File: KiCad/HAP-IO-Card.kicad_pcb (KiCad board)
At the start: 2 copper layers, 110 x 72 mm, 203 parts, among them CON601 AVR-JTAG-10, J201 TE_Connectivity_1-282834-0, J202 TE_Connectivity_282834-6, J203 TE_Connectivity_282834-6, J204 TE_Connectivity_1-282834-0, J401 TE_Connectivity_1-282834-0, J402 TE_Connectivity_282834-6, J501 TE_Connectivity_282834-3, J502 CONN_01X03_FEMALE, J601 ISP0, J602 ISP1, J603 CONN_01X02, J604 CONN_01X02, J605 CONN_01X02, J606 CONN_01X02, J607 CONN_01X03, J608 CONN_01X03, J701 5V_I/O_2, J702 5V_I/O_1, J703 NEO1, J704 NEO2, J705 NEO3, J706 NEO4, J707 CONN_01X03, Q201 ZXTN25050DFHTA, Q202 ZXTN25050DFHTA, Q203 ZXTN25050DFHTA, Q204 ZXTN25050DFHTA, Q205 ZXTN25050DFHTA, Q206 ZXTN25050DFHTA, Q207 ZXTN25050DFHTA, Q208 ZXTN25050DFHTA, U201 LTV-354T, U202 LTV-354T, U203 LTV-354T, U204 LTV-354T, U205 LTV-354T, U206 LTV-354T, U207 LTV-354T, U208 LTV-354T, U209 MCP23017, U401 ADS1115IDGST, U402 ADS1115IDGST, U501 LM1086-5V, U502 LM1086-3.3V, U701 TXB0102DCT

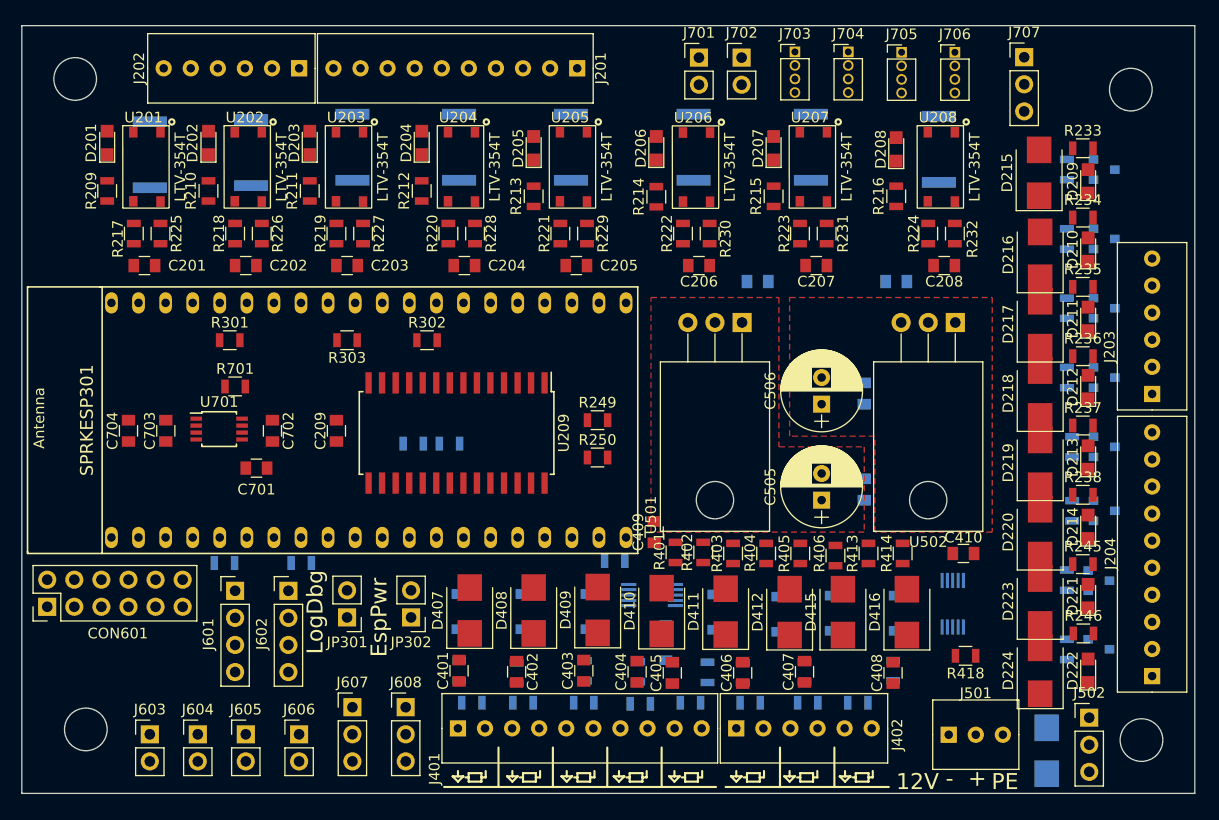
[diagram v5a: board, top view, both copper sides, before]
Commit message: Halfway through routing - need better layout to prevent rats nest
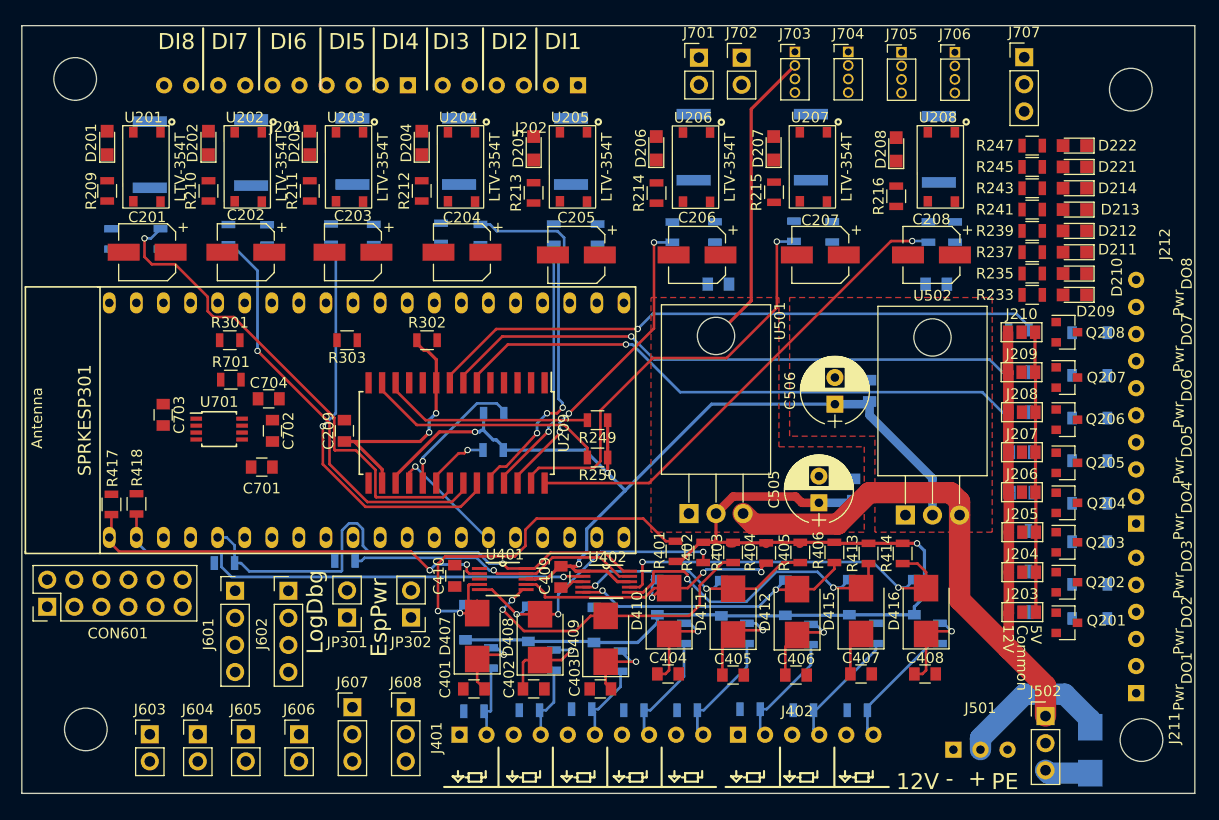
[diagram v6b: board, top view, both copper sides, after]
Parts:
- added J205: GS3, Connectors:GS3, F.Cu at (131.1, 65.0)
- added J206: GS3, Connectors:GS3, F.Cu at (131.0, 61.2)
- added J207: GS3, Connectors:GS3, F.Cu at (131.0, 57.5)
- added J208: GS3, Connectors:GS3, F.Cu at (131.0, 53.7)
- added J209: GS3, Connectors:GS3, F.Cu at (131.0, 50.0)
- added J210: GS3, Connectors:GS3, F.Cu at (131.0, 46.2)
- added J211: TE_Connectivity_282834-6, TE_Connectivity:TE_Connectivity_282834-6, F.Cu at (141.7, 80.1)
- added J212: TE_Connectivity_1-282834-0, TE_Connectivity:TE_Connectivity_1-282834-0, F.Cu at (141.7, 64.2)
- C201, C202, C203, C204, C205, C206, C207, C208: footprint Capacitors_SMD:C_0805 -> Capacitors_SMD:CP_Elec_5x4.5
- C505, C506: footprint Capacitors_THT:CP_Radial_D7.5mm_P2.50mm -> Capacitors_THT:CP_Radial_D6.3mm_P2.50mm
- D215, D216, D217, D218, D219, D220, D223, D224: value S1BB-13-F -> MBR0580; footprint Diodes_SMD:D_SMB -> Diodes_SMD:D_SOD-123; moved to B.Cu
- J203: value TE_Connectivity_282834-6 -> GS3; footprint TE_Connectivity:TE_Connectivity_282834-6 -> Connectors:GS3
- J204: value TE_Connectivity_1-282834-0 -> GS3; footprint TE_Connectivity:TE_Connectivity_1-282834-0 -> Connectors:GS3
- Q201, Q202, Q203, Q204, Q205, Q206, Q207, Q208, R417, U401, U402: moved to F.Cu
- R209, R210, R211, R212, R213, R214, R215, R216: value 180 -> 56
- R217, R218, R219, R220, R221, R222, R223, R224, R225, R226, R227, R228, R229, R230, R231, R232: moved to B.Cu
- R233, R235, R237, R245: value 180 -> 68
- R234, R236, R238, R246: value 180 -> 470; moved to B.Cu
- R239, R241, R243, R247: value 470 -> 68; moved to F.Cu
- moved R418 79.0 mm to (48.0, 62.3), turned to 270 degrees
- moved D222 49.3 mm to (136.0, 28.7), turned to 180 degrees
- moved C410 47.7 mm to (77.8, 69.1), turned to 270 degrees
- moved R417 47.5 mm to (45.6, 62.4), turned to 270 degrees
- moved Q201 42.6 mm to (135.2, 73.5)
- moved D215 42.1 mm to (137.4, 73.1), turned to 180 degrees
- moved R247 40.9 mm to (132.0, 28.7), turned to 0 degrees
- moved D221 40.3 mm to (136.0, 30.7), turned to 180 degrees
- moved R245 37.6 mm to (132.0, 30.7)
- moved R234 37.5 mm to (130.8, 72.5)
- moved U402 32.6 mm to (92.0, 69.6), turned to 0 degrees
- moved Q202 32.4 mm to (135.2, 69.7)
- moved D224 32.0 mm to (137.4, 46.3), turned to 180 degrees
- moved D214 31.8 mm to (136.0, 32.7), turned to 180 degrees
- moved D216 31.2 mm to (137.4, 69.9), turned to 180 degrees
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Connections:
- net /Powersupply/Input12VOutside renamed /Powersupply/12V_PWR
- C501 pad 1: /Powersupply/Input12V -> +12V
- C502 pad 1: /Powersupply/Input12V -> +12V
- D501 pad 1: +12V -> Net-(D501-Pad1)
- J203 pad 1: Earth -> POWER5V
- J203 pad 2: /Digital I/O/DO_1 -> /Digital I/O/PWR_DO_1
- J203 pad 3: Earth -> +12V
- J204 pad 1: Earth -> POWER5V
- J204 pad 2: /Digital I/O/DO_4 -> /Digital I/O/PWR_DO_2
- J204 pad 3: Earth -> +12V
- J502 pad 1: /Powersupply/Input12V -> +12V
- J502 pad 3: +12V -> Net-(D501-Pad1)
- R234 pad 1: POWER3V3 -> Net-(Q201-Pad1)
- R234 pad 2: Net-(D210-Pad2) -> DO1
- R235 pad 2: Net-(D211-Pad2) -> Net-(D210-Pad2)
- R236 pad 1: POWER3V3 -> Net-(Q202-Pad1)
- R236 pad 2: Net-(D212-Pad2) -> DO2
- R237 pad 2: Net-(D213-Pad2) -> Net-(D211-Pad2)
- R238 pad 1: POWER3V3 -> Net-(Q203-Pad1)
- R238 pad 2: Net-(D214-Pad2) -> DO3
- R239 pad 1: Net-(Q201-Pad1) -> POWER3V3
- R239 pad 2: DO1 -> Net-(D212-Pad2)
- R240 pad 1: Net-(Q202-Pad1) -> Net-(Q204-Pad1)
- R240 pad 2: DO2 -> DO4
- R241 pad 1: Net-(Q203-Pad1) -> POWER3V3
- R241 pad 2: DO3 -> Net-(D213-Pad2)
- R242 pad 1: Net-(Q204-Pad1) -> Net-(Q205-Pad1)
- R242 pad 2: DO4 -> DO5
- R243 pad 1: Net-(Q205-Pad1) -> POWER3V3
- R243 pad 2: DO5 -> Net-(D214-Pad2)
- R246 pad 1: POWER3V3 -> Net-(Q207-Pad1)
- R246 pad 2: Net-(D222-Pad2) -> DO7
- R247 pad 1: Net-(Q207-Pad1) -> POWER3V3
- R247 pad 2: DO7 -> Net-(D222-Pad2)
- U501 pad 3: /Powersupply/Input12V -> +12V
- U502 pad 3: /Powersupply/Input12V -> +12V
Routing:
- net POWER5V: track 0.00 -> 147.5 mm, vias 0 -> 1
- net POWER3V3: track 0.00 -> 117.8 mm, vias 0 -> 5
- net +12V: track 0.00 -> 75.5 mm
- net DO8: track 0.00 -> 58.2 mm, vias 0 -> 1
- net DO7: track 0.00 -> 54.7 mm, vias 0 -> 1
- net DO6: track 0.00 -> 54.4 mm, vias 0 -> 1
- net SENSE_SCL: track 0.00 -> 49.4 mm, vias 0 -> 1
- net SENSE_RDY_2: track 0.00 -> 46.6 mm, vias 0 -> 1
- net DI1: track 0.00 -> 46.5 mm, vias 0 -> 1
- net DI8: track 0.00 -> 45.4 mm, vias 0 -> 1
- net DI7: track 0.00 -> 40.9 mm, vias 0 -> 1
- net Sense1: track 0.00 -> 40.2 mm, vias 0 -> 2
- net DI2: track 0.00 -> 39.8 mm, vias 0 -> 1
- net SENSE_RDY_1: track 0.00 -> 39.4 mm, vias 0 -> 2
- net DI3: track 0.00 -> 38.8 mm, vias 0 -> 1
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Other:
- net class 12V added: clearance 0.2, trace_width 1, via_dia 0.6, via_drill 0.4
- net class 3V3: trace_width 0.25 -> 0.3
- net class 5V: trace_width 0.25 -> 0.3
- net class Earth added: clearance 0.2, trace_width 0.25, via_dia 0.6, via_drill 0.4
- net class Input12V removed
- net class Input12VOutside removed
- net class Input12VOutside2 removed
- board text added: "5V"
- board text added: "Common"
- board text added: "DI1"
- board text added: "DI2"
- board text added: "DI3"
- board text added: "DI4"
- board text added: "DI5"
- board text added: "DI6"
- board text added: "DI7"
- board text added: "DI8"
- board text added: "DO1"
- board text added: "DO2"
- board text added: "DO3"
- board text added: "DO4"
- board text added: "DO5"
- board text added: "DO6"
- board text added: "DO7"
- board text added: "DO8"
- board text added: "Pwr"

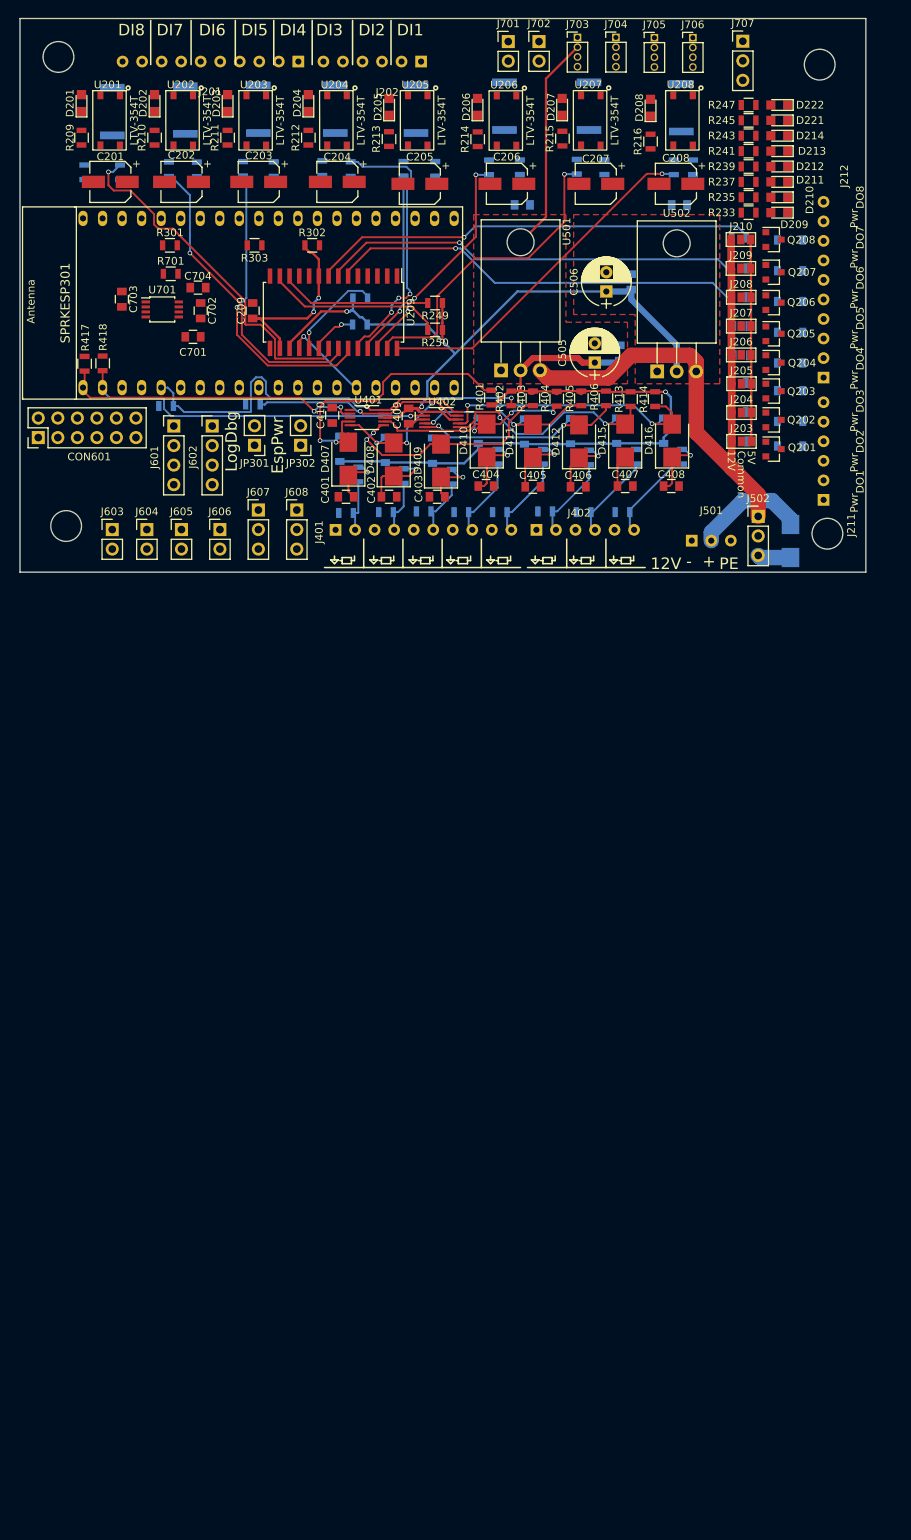
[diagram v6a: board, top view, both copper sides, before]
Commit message: New sense input circuits. New layout
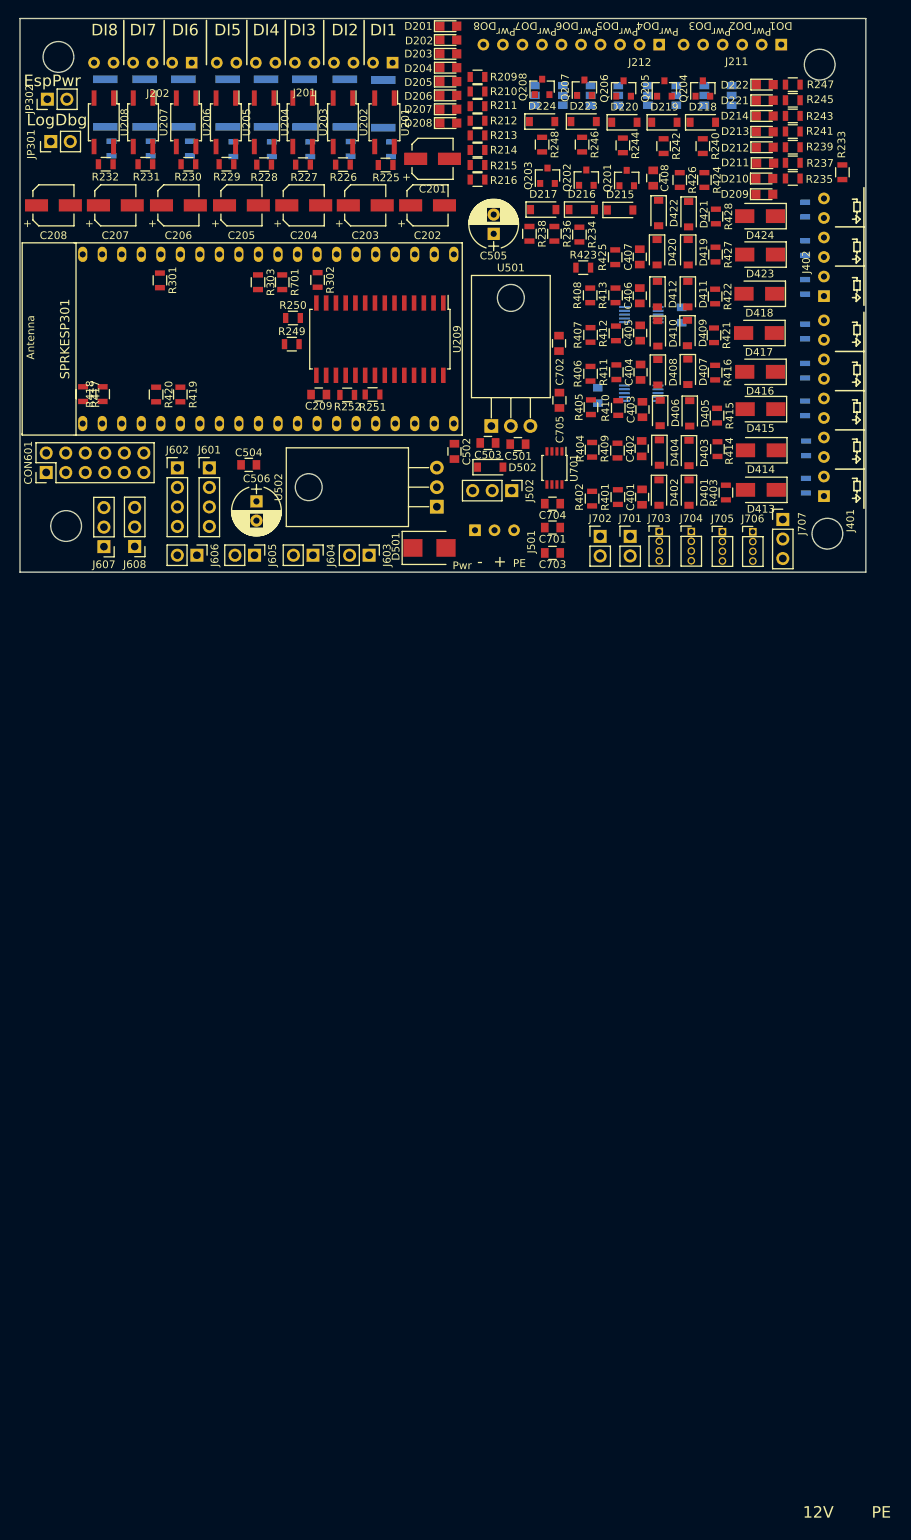
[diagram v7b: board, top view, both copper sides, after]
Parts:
- removed the R412 at (111.2, 74.6)
- added C705: 100nF, Capacitors_SMD:C_0805, F.Cu at (107.4, 67.1)
- added D417: D, Diodes_SMD:D_SMA, F.Cu at (133.3, 58.4)
- added D418: D, Diodes_SMD:D_SMA, F.Cu at (133.4, 53.3)
- added D419: D_Schottky, Diodes_SMD:D_SOD-123, F.Cu at (124.1, 47.9)
- added D420: D_Schottky, Diodes_SMD:D_SOD-123, F.Cu at (120.1, 47.9)
- added D421: D_Schottky, Diodes_SMD:D_SOD-123, F.Cu at (124.2, 42.9)
- added D422: D_Schottky, Diodes_SMD:D_SOD-123, F.Cu at (120.3, 42.8)
- added D423: D, Diodes_SMD:D_SMA, F.Cu at (133.5, 48.2)
- added D424: D, Diodes_SMD:D_SMA, F.Cu at (133.5, 43.2)
- added D502: D_Zener, Diodes_SMD:D_SOD-123, F.Cu at (98.4, 75.8)
- added J401: TE_Connectivity_1-282834-0, TE_Connectivity:TE_Connectivity_1-282834-0, F.Cu at (141.8, 79.6)
- added R421: 1k, Resistors_SMD:R_0805, F.Cu at (127.5, 58.7)
- added R422: 1k, Resistors_SMD:R_0805, F.Cu at (127.6, 53.6)
- added R423: 100, Resistors_SMD:R_0805, F.Cu at (110.5, 49.9)
- added R424: 100, Resistors_SMD:R_0805, F.Cu at (126.2, 38.5)
- added R425: 2k, Resistors_SMD:R_0805, F.Cu at (114.6, 48.5)
- added R426: 2k, Resistors_SMD:R_0805, F.Cu at (123.0, 38.5)
- added R427: 1k, Resistors_SMD:R_0805, F.Cu at (127.7, 48.2)
- added R428: 1k, Resistors_SMD:R_0805, F.Cu at (127.7, 43.2)
- C409, C410, J203, J204, J205, J206, J207, J208, J209, J210, U401, U402: moved to B.Cu
- C501, C502, C503, C504, D215, D216, D217, D218, D219, D220, D223, D224, D401, D402, D403, D404, D405, D406, D501, R225, R226, R227, R228, R229, R230, R231, R232, R234, R236, R238, R240, R242, R244, R246, R248, R251, R252, R419, R420: moved to F.Cu
- D407, D408, D409, D410, D411, D412: value S1BB-13-F -> D_Schottky; footprint Diodes_SMD:D_SMB -> Diodes_SMD:D_SOD-123
- D413, D414: value D_Schottky -> D; footprint Diodes_SMD:D_SOD-123 -> Diodes_SMD:D_SMA; moved to F.Cu
- D415, D416: value S1BB-13-F -> D; footprint Diodes_SMD:D_SMB -> Diodes_SMD:D_SMA
- R402, R404, R405, R406: value 2k -> 100
- R403, R414: value 2k -> 1k
- R407, R408: value 499 -> 100; moved to F.Cu
- R409, R410, R411: value 499 -> 2k; moved to F.Cu
- R412: renamed from J401; value TE_Connectivity_1-282834-0 -> 2k; footprint TE_Connectivity:TE_Connectivity_1-282834-0 -> Resistors_SMD:R_0805
- R415, R416: value 499 -> 1k; moved to F.Cu
- U201, U202, U203, U204, U205, U206, U207, U208: footprint LTV-354T_MiniFlat:LTV-354T_MiniFlat -> Housings_SOIC:SO-4_4.4x3.6mm_Pitch2.54mm
- moved C208 81.0 mm to (41.6, 41.8), turned to 0 degrees
- moved U208 76.7 mm to (48.1, 31.0), turned to 270 degrees
- moved R232 76.4 mm to (48.4, 36.4), turned to 0 degrees
- moved R208 74.9 mm to (48.3, 28.5)
- moved R224 73.2 mm to (49.1, 34.4), turned to 270 degrees
- moved J701 66.3 mm to (116.6, 84.8)
- moved J703 65.1 mm to (120.4, 84.2)
- moved C703 65.0 mm to (106.5, 87.0), turned to 180 degrees
- moved J704 65.0 mm to (124.5, 84.2)
- moved J705 64.8 mm to (128.6, 84.2)
- moved J702 64.8 mm to (112.7, 84.8)
- moved J706 64.7 mm to (132.5, 84.2)
- moved C207 62.5 mm to (49.6, 41.8), turned to 0 degrees
- moved J707 62.4 mm to (136.4, 82.6)
- moved RV401 59.9 mm to (139.4, 78.2), turned to 90 degrees
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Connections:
- C401 pad 1: Net-(C401-Pad1) -> Earth
- C401 pad 2: Earth -> Net-(C401-Pad2)
- C402 pad 1: Net-(C402-Pad1) -> Earth
- C402 pad 2: Earth -> Net-(C402-Pad2)
- C403 pad 1: Net-(C403-Pad1) -> Earth
- C403 pad 2: Earth -> Net-(C403-Pad2)
- C404 pad 1: Net-(C404-Pad1) -> Earth
- C404 pad 2: Earth -> Net-(C404-Pad2)
- C405 pad 1: Net-(C405-Pad1) -> Earth
- C405 pad 2: Earth -> Net-(C405-Pad2)
- C406 pad 1: Net-(C406-Pad1) -> Earth
- C406 pad 2: Earth -> Net-(C406-Pad2)
- C407 pad 1: Net-(C407-Pad1) -> Earth
- C407 pad 2: Earth -> Net-(C407-Pad2)
- C408 pad 1: Net-(C408-Pad1) -> Earth
- C408 pad 2: Earth -> Net-(C408-Pad2)
- D401 pad 2: Sense1 -> Net-(C401-Pad2)
- D402 pad 1: POWER5V -> Net-(C401-Pad2)
- D402 pad 2: Sense2 -> Earth
- D403 pad 2: Sense3 -> Net-(C402-Pad2)
- D404 pad 1: POWER5V -> Net-(C402-Pad2)
- D404 pad 2: Sense4 -> Earth
- D405 pad 2: Sense5 -> Net-(C403-Pad2)
- D406 pad 1: POWER5V -> Net-(C403-Pad2)
- D406 pad 2: Sense6 -> Earth
- D407 pad 1: Net-(C401-Pad1) -> POWER5V
- D407 pad 2: Sense1 -> Net-(C404-Pad2)
- D408 pad 1: Net-(C402-Pad1) -> Net-(C404-Pad2)
- D408 pad 2: Sense2 -> Earth
- D409 pad 1: Net-(C403-Pad1) -> POWER5V
- D409 pad 2: Sense3 -> Net-(C405-Pad2)
- D410 pad 1: Net-(C404-Pad1) -> Net-(C405-Pad2)
- D410 pad 2: Sense4 -> Earth
- D411 pad 1: Net-(C405-Pad1) -> POWER5V
- D411 pad 2: Sense5 -> Net-(C406-Pad2)
- D412 pad 1: Net-(C406-Pad1) -> Net-(C406-Pad2)
- D412 pad 2: Sense6 -> Earth
- D413 pad 1: POWER5V -> /Sense Inputs/Sense1_DUT
- D413 pad 2: Sense7 -> Earth
- D414 pad 1: POWER5V -> /Sense Inputs/Sense2_DUT
- D414 pad 2: Sense8 -> Earth
- D415 pad 1: Net-(C407-Pad1) -> /Sense Inputs/Sense3_DUT
- D415 pad 2: Sense7 -> Earth
- D416 pad 1: Net-(C408-Pad1) -> /Sense Inputs/Sense4_DUT
- D416 pad 2: Sense8 -> Earth
- J701 pad 2: Net-(C703-Pad1) -> Net-(C704-Pad1)
- J702 pad 2: Net-(C704-Pad1) -> Net-(C703-Pad1)
- R401 pad 2: Sense1 -> Net-(C401-Pad2)
- R402 pad 1: POWER5V -> Sense1
- R402 pad 2: Sense2 -> Net-(C401-Pad2)
- R403 pad 1: POWER5V -> /Sense Inputs/Sense1_DUT
- R403 pad 2: Sense3 -> Net-(C401-Pad2)
- R404 pad 1: POWER5V -> Sense2
- R404 pad 2: Sense4 -> Net-(C402-Pad2)
- R405 pad 1: POWER5V -> Sense3
- R405 pad 2: Sense5 -> Net-(C403-Pad2)
- R406 pad 1: POWER5V -> Sense4
- R406 pad 2: Sense6 -> Net-(C404-Pad2)
- R407 pad 1: /Sense Inputs/Sense1_DUT -> Sense5
- R407 pad 2: Net-(C401-Pad1) -> Net-(C405-Pad2)
- R408 pad 1: /Sense Inputs/Sense2_DUT -> Sense6
- R408 pad 2: Net-(C402-Pad1) -> Net-(C406-Pad2)
- R409 pad 1: /Sense Inputs/Sense3_DUT -> POWER5V
- R409 pad 2: Net-(C403-Pad1) -> Net-(C402-Pad2)
- R410 pad 1: /Sense Inputs/Sense4_DUT -> POWER5V
- R410 pad 2: Net-(C404-Pad1) -> Net-(C403-Pad2)
- R411 pad 1: /Sense Inputs/Sense5_DUT -> POWER5V
- R411 pad 2: Net-(C405-Pad1) -> Net-(C404-Pad2)
- R412 pad 1: Earth -> POWER5V
- R412 pad 2: /Sense Inputs/Sense1_DUT -> Net-(C405-Pad2)
- R413 pad 2: Sense7 -> Net-(C406-Pad2)
- R414 pad 1: POWER5V -> /Sense Inputs/Sense2_DUT
- R414 pad 2: Sense8 -> Net-(C402-Pad2)
- R415 pad 1: /Sense Inputs/Sense7_DUT -> /Sense Inputs/Sense3_DUT
- R415 pad 2: Net-(C407-Pad1) -> Net-(C403-Pad2)
- R416 pad 1: /Sense Inputs/Sense8_DUT -> /Sense Inputs/Sense4_DUT
- R416 pad 2: Net-(C408-Pad1) -> Net-(C404-Pad2)
- U201 pad 2: Net-(U201-Pad2) -> /Digital I/O/DI1_2
- U201 pad 3: /Digital I/O/DI1_2 -> Earth
- U201 pad 4: Earth -> DI1
- U202 pad 2: Net-(U202-Pad2) -> /Digital I/O/DI2_2
- U202 pad 3: /Digital I/O/DI2_2 -> Earth
- U202 pad 4: Earth -> DI2
- U203 pad 2: Net-(U203-Pad2) -> /Digital I/O/DI3_2
- U203 pad 3: /Digital I/O/DI3_2 -> Earth
- U203 pad 4: Earth -> DI3
- U204 pad 2: Net-(U204-Pad2) -> /Digital I/O/DI4_2
- U204 pad 3: /Digital I/O/DI4_2 -> Earth
- U204 pad 4: Earth -> DI4
- U205 pad 2: Net-(U205-Pad2) -> /Digital I/O/DI5_2
- U205 pad 3: /Digital I/O/DI5_2 -> Earth
- U205 pad 4: Earth -> DI5
- U206 pad 2: Net-(U206-Pad2) -> /Digital I/O/DI6_2
- U206 pad 3: /Digital I/O/DI6_2 -> Earth
- U206 pad 4: Earth -> DI6
- U207 pad 2: Net-(U207-Pad2) -> /Digital I/O/DI7_2
- U207 pad 3: /Digital I/O/DI7_2 -> Earth
- U207 pad 4: Earth -> DI7
- U208 pad 2: Net-(U208-Pad2) -> /Digital I/O/DI8_2
- U208 pad 3: /Digital I/O/DI8_2 -> Earth
- U208 pad 4: Earth -> DI8
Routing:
- net POWER5V: track 147.5 -> 0.00 mm, vias 1 -> 0
- net POWER3V3: track 117.8 -> 0.00 mm, vias 5 -> 0
- net +12V: track 75.5 -> 0.00 mm
- net DO8: track 58.2 -> 0.00 mm, vias 1 -> 0
- net DO7: track 54.7 -> 0.00 mm, vias 1 -> 0
- net DO6: track 54.4 -> 0.00 mm, vias 1 -> 0
- net SENSE_SCL: track 49.4 -> 0.00 mm, vias 1 -> 0
- net SENSE_RDY_2: track 46.6 -> 0.00 mm, vias 1 -> 0
- net DI1: track 46.5 -> 0.00 mm, vias 1 -> 0
- net DI8: track 45.4 -> 0.00 mm, vias 1 -> 0
- net DI7: track 40.9 -> 0.00 mm, vias 1 -> 0
- net Sense1: track 40.2 -> 0.00 mm, vias 2 -> 0
- net DI2: track 39.8 -> 0.00 mm, vias 1 -> 0
- net SENSE_RDY_1: track 39.4 -> 0.00 mm, vias 2 -> 0
- net DI3: track 38.8 -> 0.00 mm, vias 1 -> 0
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- removed copper zone on F.Cu, net POWER3V3
- removed copper zone on F.Cu, net POWER5V
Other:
- net class 12V: clearance 0.2 -> 0.3; trace_width 1 -> 0.4
- net class Sens added: clearance 0.2, trace_width 0.25, via_dia 0.6, via_drill 0.4
- board text added: "PerMalmberg @ GitHub"
- board text removed: "HAP I/O Card (C) Per Malmberg"
